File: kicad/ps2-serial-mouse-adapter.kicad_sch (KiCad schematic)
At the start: 8 parts, among them U1 Arduino_Nano, U2 MAX3232_HW027

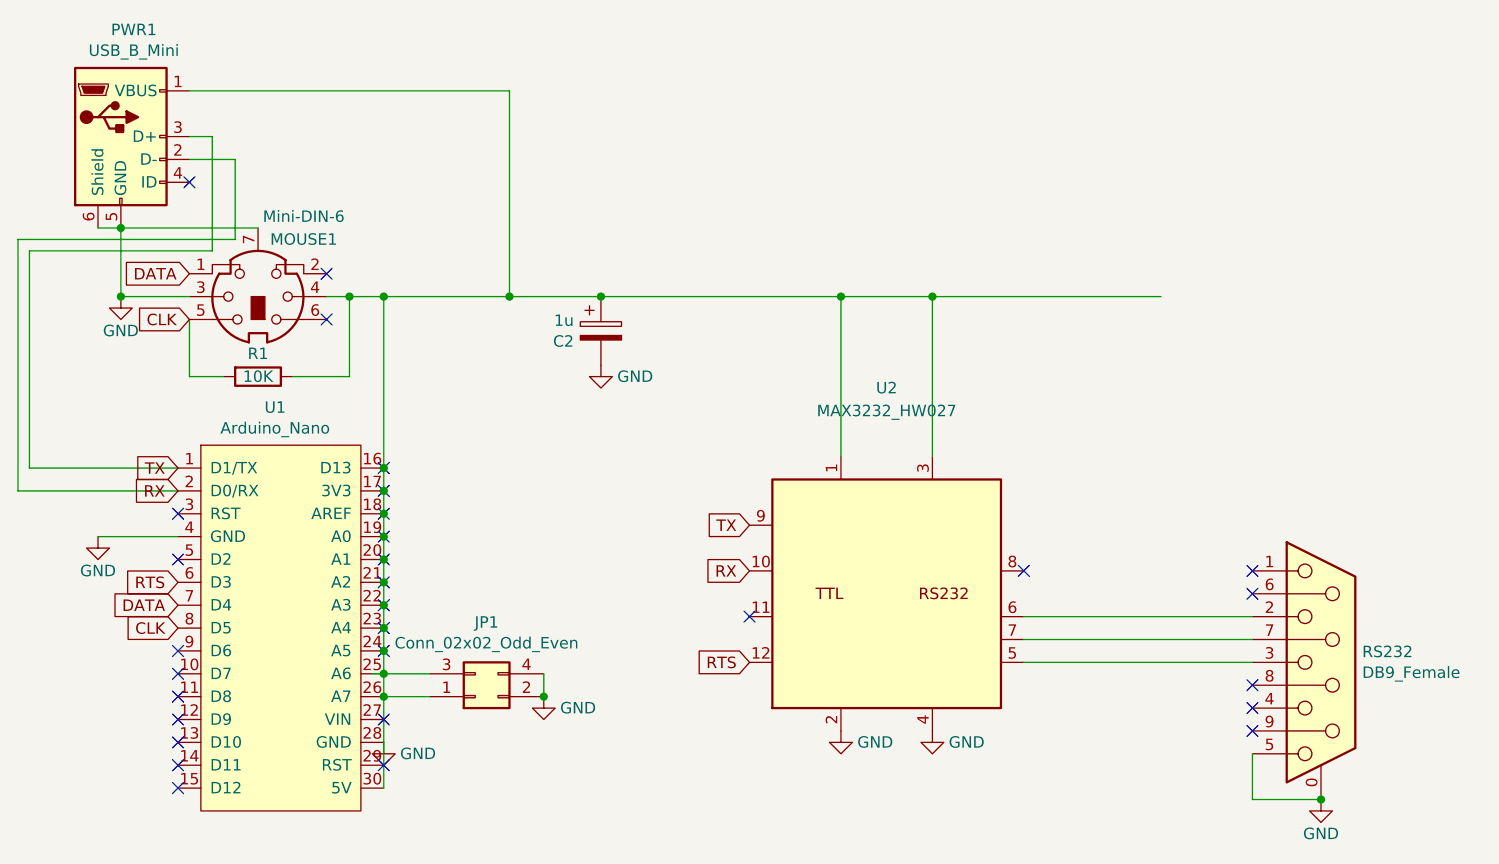
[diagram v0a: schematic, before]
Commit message: Improve trace routing for better printing and fix net assignments
- Rerouted traces for cleaner print output
- Fixed VBUS and jumper net assignments (were incorrectly marked unconnected)
- Expand .gitignore to exclude KiCad autosave, lock, cache, history, and .kicad_prl
- Untrack .kicad_prl (machine-specific local preferences)

Co-Authored-By: Claude Sonnet 4.6 <noreply@anthropic.com>
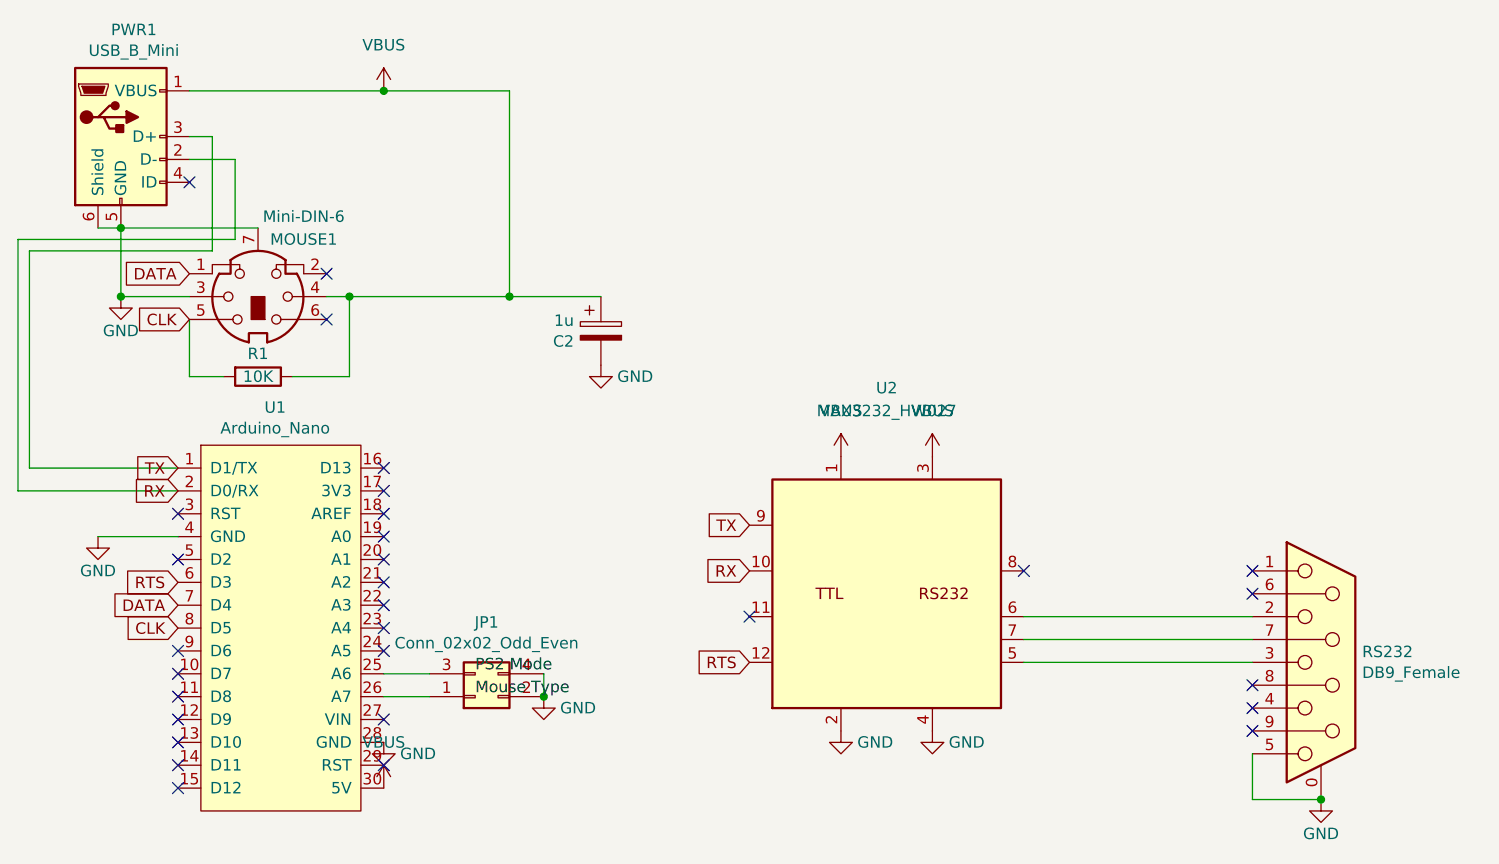
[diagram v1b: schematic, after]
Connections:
- new net: JP1.3 (Pin_3), U1.25 (A6)
- new net: JP1.1 (Pin_1), U1.26 (A7)
- new net VBUS: C2.1, MOUSE1.4, PWR1.1 (VBUS), R1.1, U1.30 (5V), U2.1 (VCC), U2.3 (VCC2)
- now unconnected: U1.16 (D13), U1.17 (3V3), U1.18 (AREF), U1.19 (A0), U1.20 (A1), U1.21 (A2), U1.22 (A3), U1.23 (A4), U1.24 (A5)
